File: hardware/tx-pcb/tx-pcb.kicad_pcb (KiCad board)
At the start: 4 copper layers, 83.4 x 79.1 mm, 66 parts, among them J1 Conn_To_J1, J2 Conn_To_J2, J3 BLIO, J4 Conn_01x05, J5 Conn_01x04, J6 PWRO, J7 Conn_01x02_Pin, SW1 BOOT0, SW2 RESET, SW3 BTN1, SW4 BTN2, SW5 BTN3, SW6 BTN4, SW7 BTN5, SW8 SW_SPDT, U1 USBLC6-2SC6, U2 STM32WB55CEUx, X1 CS11336-32M, X2 ABS07-32.768KHZ-1-T

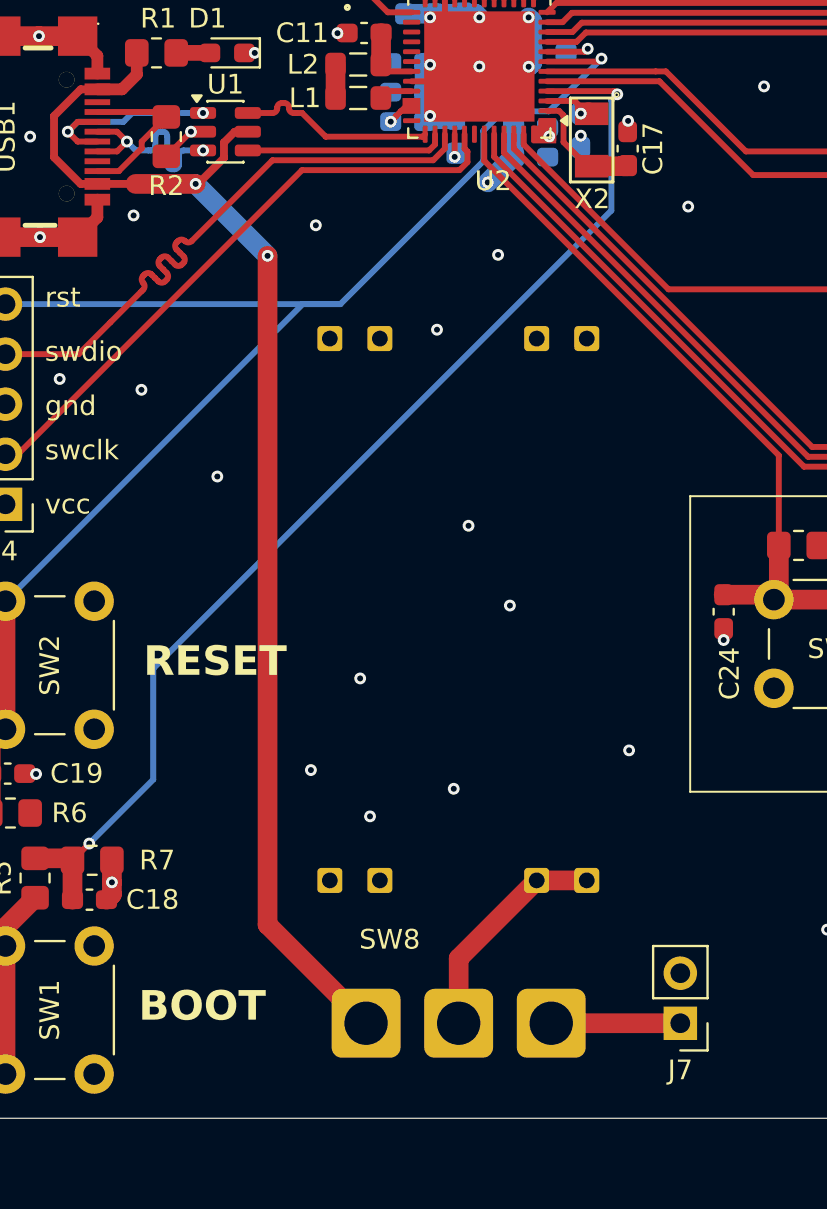
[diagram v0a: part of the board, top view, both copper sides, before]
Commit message: updated power switch for tx board
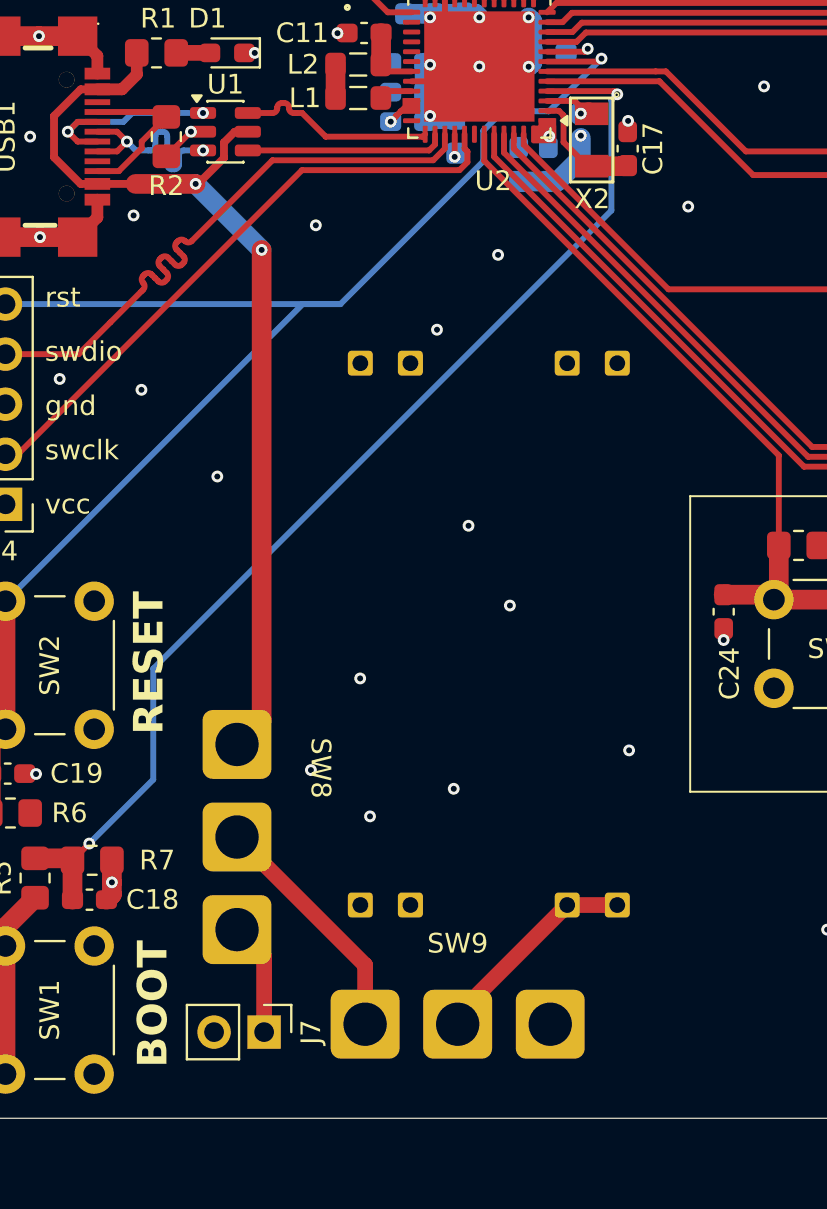
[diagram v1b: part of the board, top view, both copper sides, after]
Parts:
- added SW9: SW_SPDT, rf-pwr-tx-library:spdt_amazon, F.Cu at (146.7, 135.3)
- moved J7 21.1 mm to (136.9, 135.7), turned to -90 degrees
- moved SW8 14.7 mm to (135.5, 125.8), turned to 90 degrees
- moved U3 1.99 mm to (148.3, 115.5)
- moved C6 1.97 mm to (149.8, 91.7), turned to -90 degrees
- moved C5 0.97 mm to (151.3, 91.7), turned to -90 degrees
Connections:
- SW8 pad 2: /reg_in -> Net-(SW8-B)
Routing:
- net /VBUS: track 66.4 -> 50.6 mm
- net Net-(SW8-B): track 0.00 -> 12.2 mm
- net GND: track 45.3 -> 46.6 mm, vias 47 -> 46
- net Net-(J7-Pin_1): track 6.55 -> 5.77 mm
- net /reg_in: track 11.4 -> 10.9 mm

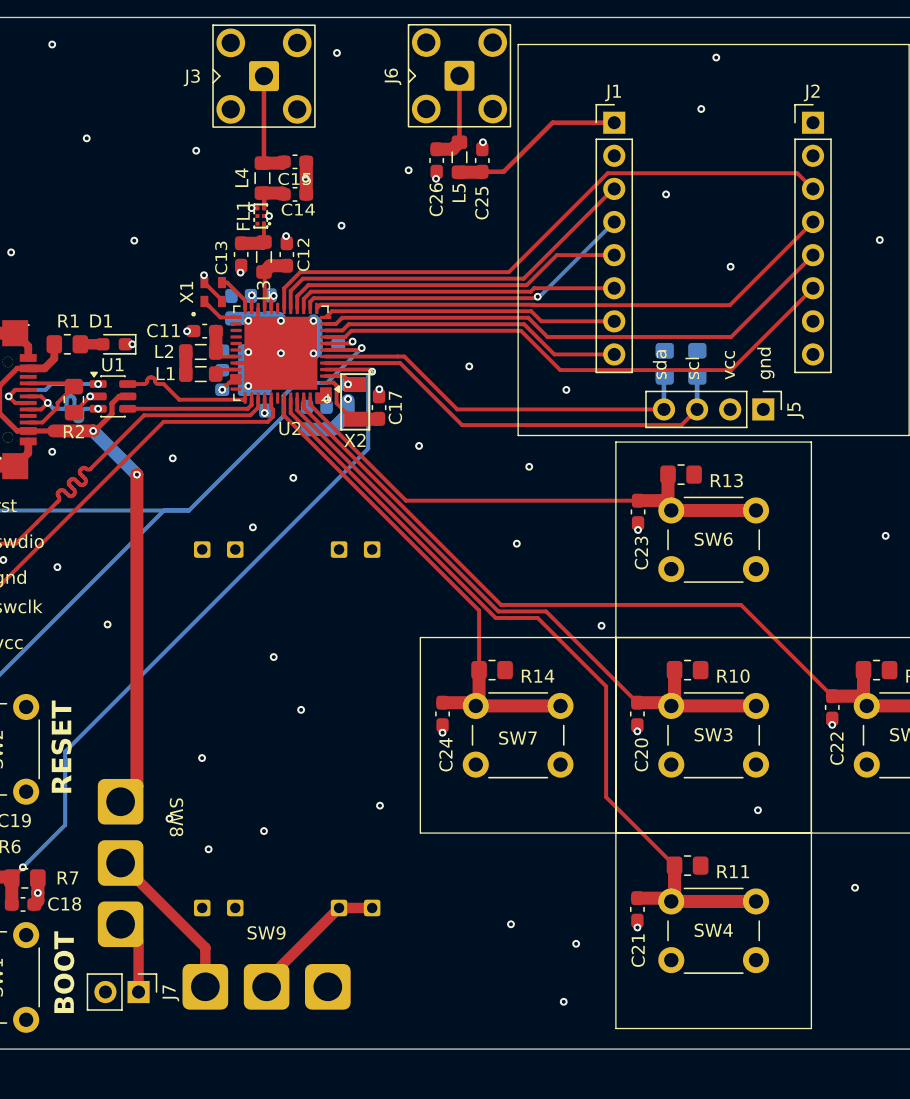
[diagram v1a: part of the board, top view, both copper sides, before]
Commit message: double checked for purchase
updated TX SPI_CLK pin, was incorrect
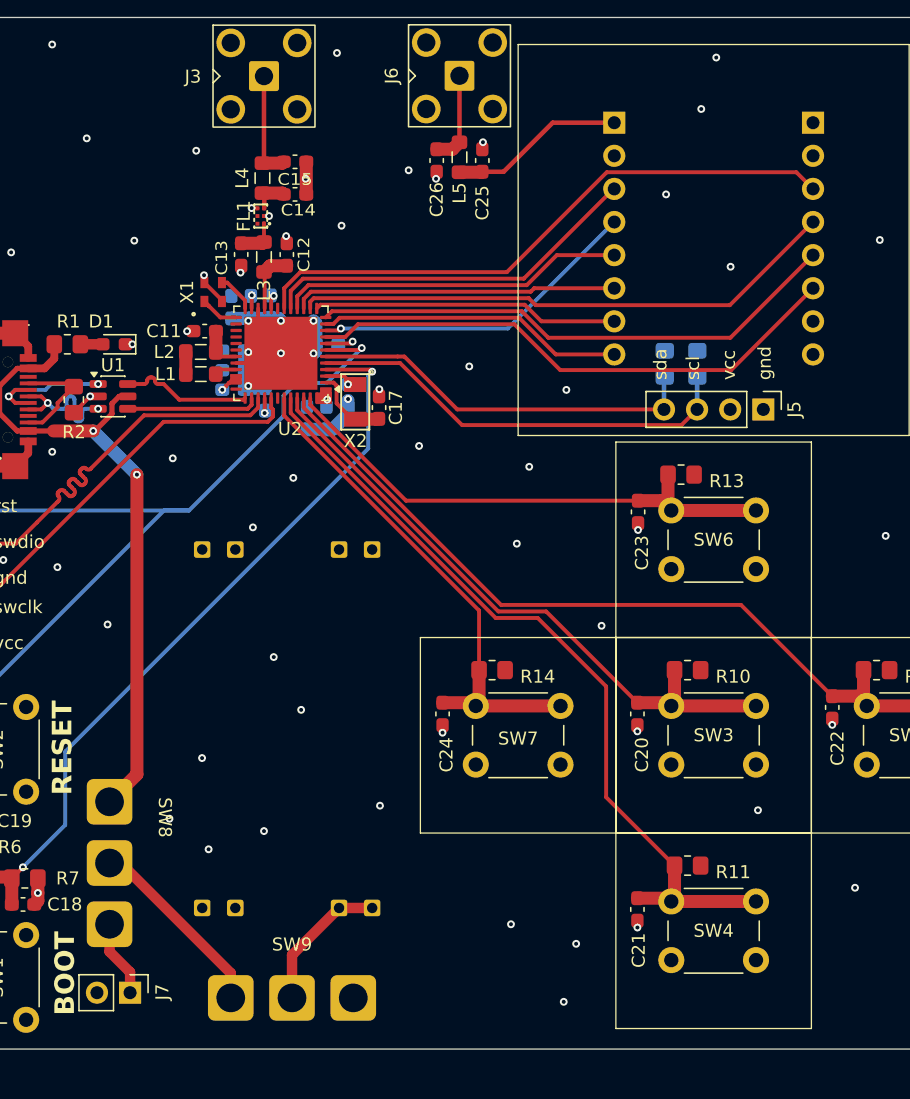
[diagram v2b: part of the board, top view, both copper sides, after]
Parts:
- J1, J2: moved to B.Cu
- moved SW9 2.13 mm to (148.7, 136.2)
- moved SW8 0.85 mm to (134.7, 125.8)
- moved J7 0.65 mm to (136.2, 135.8)
- turned J1 to 180 degrees
- turned J2 to 180 degrees
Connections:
- U2 pad 10: /SX1262_BUSY -> /SPI_SCK
- U2 pad 11: /SX1262_DIO2 -> /SX1262_BUSY
- U2 pad 12: /SX1262_RST -> /SX1262_DIO2
- U2 pad 13: /SX1262_RFSW -> /SX1262_RST
- U2 pad 14: /SPI_SCK -> /SX1262_RFSW
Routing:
- net Net-(SW8-B): track 12.2 -> 13.9 mm
- net /SX1262_RFSW: track 40.9 -> 42.1 mm
- net /SX1262_RST: track 22.7 -> 23.5 mm
- net /SPI_SCK: track 26.4 -> 25.6 mm

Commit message: updates immediately pre JLC
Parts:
- moved J7 14.2 mm to (150.4, 135.2), turned to 0 degrees
- moved SW9 11.7 mm to (160.4, 135.8)
- moved SW8 11.4 mm to (140.2, 135.8), turned to 180 degrees
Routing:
- net /VBUS: track 50.6 -> 65.2 mm
- net Net-(SW8-B): track 13.9 -> 18.0 mm
- net /reg_in: track 10.9 -> 11.7 mm
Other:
- board text added: "-"
- board text added: "BAT"
- board text added: "O"
- board text added: "USB"

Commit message: updates for dr weeks
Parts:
- removed D1: LED, LED_SMD:LED_0603_1608Metric_Pad1.05x0.95mm_HandSolder
- removed R1: 10k, Resistor_SMD:R_0805_2012Metric_Pad1.20x1.40mm_HandSolder
- removed R2: 5k1, Resistor_SMD:R_0805_2012Metric_Pad1.20x1.40mm_HandSolder
- removed SW8: SW_SPDT, rf-pwr-tx-library:spdt_amazon
- removed U1: USBLC6-2SC6, Package_TO_SOT_SMD:SOT-23-6
- removed USB1: GT-USB-7047A, rf-pwr-tx-library:USB-C-SMD_GT-USB-7047A
- moved U3 36.5 mm to (181.1, 131.6), turned to 180 degrees
- moved J7 12.5 mm to (162.8, 135.2)
- moved C18 8.61 mm to (136.6, 129.0)
- moved J4 8.61 mm to (132.4, 108.9)
- moved R5 8.61 mm to (133.9, 127.9)
- moved R6 8.61 mm to (132.6, 124.6)
- moved SW1 8.61 mm to (132.4, 137.8)
- moved SW2 8.61 mm to (132.4, 120.3)
- moved C19 8.61 mm to (132.5, 122.6)
- moved R7 8.61 mm to (136.8, 127.0)
- moved SW9 7.75 mm to (152.6, 135.8)
- moved C6 1.81 mm to (149.8, 89.9), turned to 90 degrees
- moved C5 1.81 mm to (151.3, 89.9), turned to 90 degrees
- moved C2 0.76 mm to (146.6, 89.5)
- moved C1 0.35 mm to (151.3, 85.6)
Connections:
- SW9 pad 3: Net-(SW8-B) -> Net-(J7-Pin_1)
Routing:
- net /VBUS: track 65.2 -> 0.00 mm, vias 2 -> 0
- net GND: track 46.6 -> 26.9 mm, vias 46 -> 39
- net Net-(SW8-B): track 18.0 -> 0.00 mm
- net /SWD_NSRT: track 73.4 -> 61.1 mm
- net /SWDIO: track 30.9 -> 18.7 mm
- net /reg_in: track 11.7 -> 0.00 mm
- net Net-(USB1-DN1): track 10.7 -> 0.00 mm, vias 2 -> 0
- net Net-(USB1-DP1): track 10.6 -> 0.00 mm, vias 2 -> 0
- net /USB_DP: track 10.1 -> 0.00 mm
- net /USB_DM: track 10.1 -> 0.00 mm
- net /SWCLK: track 31.1 -> 22.5 mm
- net Net-(USB1-CC1): track 8.44 -> 0.00 mm
- net Net-(J7-Pin_1): track 5.74 -> 0.00 mm
- net /BTN2: track 62.0 -> 65.7 mm
- net /BOOT0: track 57.9 -> 54.4 mm
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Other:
- board size 83.4 x 79.1 mm -> 74.3 x 79.1 mm
- board text removed: "BAT"
- board text removed: "USB"

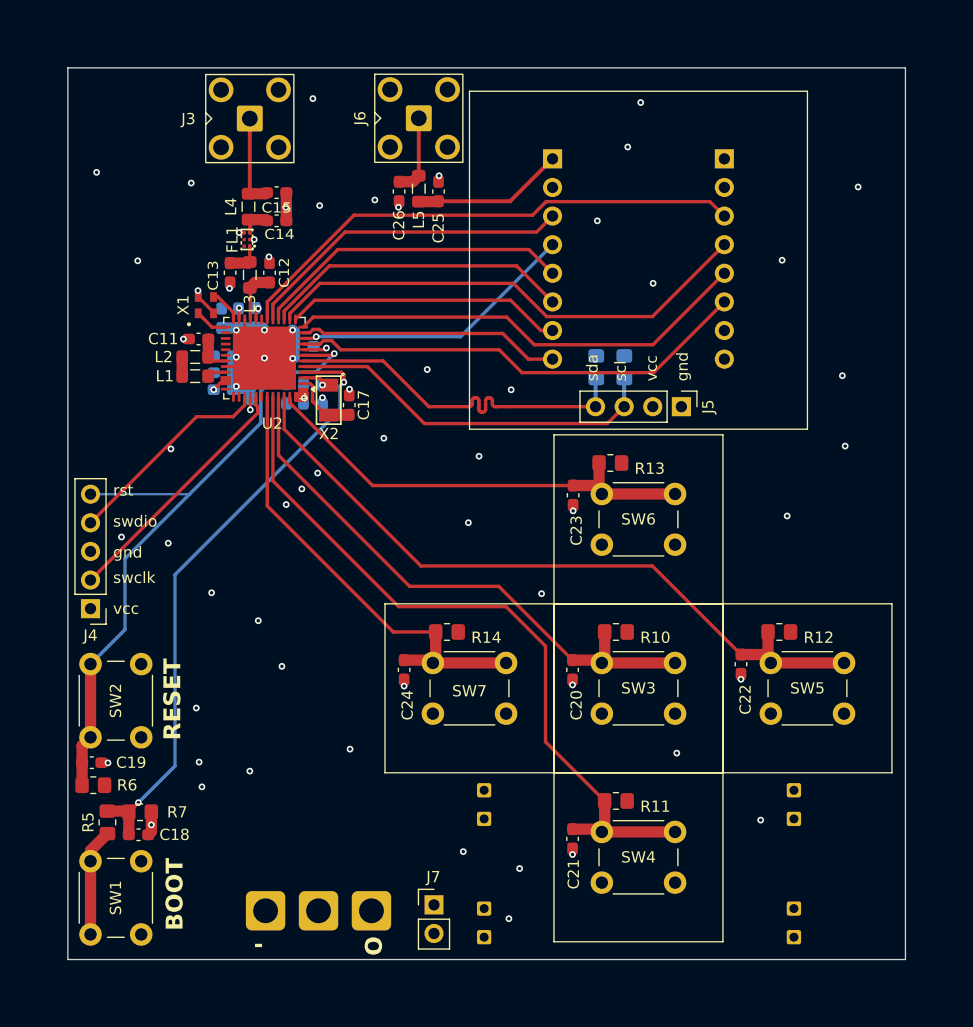
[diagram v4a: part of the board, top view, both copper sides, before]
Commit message: updated PCB for weeks purchase
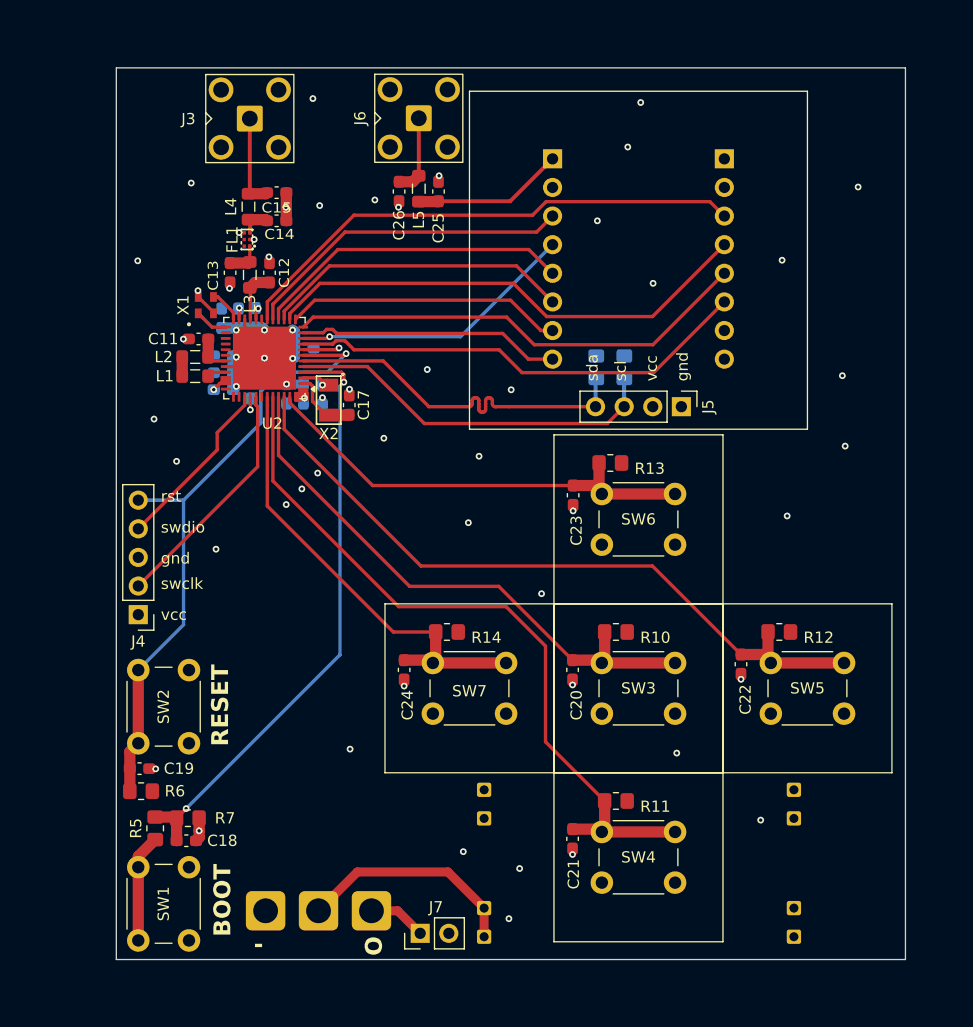
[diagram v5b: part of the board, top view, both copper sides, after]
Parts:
- moved C18 4.27 mm to (140.9, 129.5)
- moved C19 4.27 mm to (136.7, 123.1)
- moved R7 4.27 mm to (141.0, 127.5)
- moved R5 4.27 mm to (138.1, 128.4)
- moved R6 4.27 mm to (136.8, 125.1)
- moved SW1 4.27 mm to (136.6, 138.4)
- moved SW2 4.27 mm to (136.6, 120.9)
- moved J4 4.27 mm to (136.6, 109.5)
- moved J7 2.81 mm to (161.6, 137.8), turned to 90 degrees
- moved C1 0.16 mm to (151.3, 85.8)
- moved C2 0.06 mm to (146.6, 89.4)
- turned SW9 to 0 degrees
- turned U3 to 0 degrees
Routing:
- net /reg_in: track 0.00 -> 20.0 mm
- net Net-(J7-Pin_1): track 0.00 -> 5.15 mm
- net /SWD_NSRT: track 61.1 -> 57.2 mm
- net /SWDIO: track 18.7 -> 15.6 mm
- net GND: track 26.9 -> 28.5 mm, vias 39 -> 36
- net /BOOT0: track 54.4 -> 53.2 mm
- net /SWCLK: track 22.5 -> 21.3 mm
- net +3V3: track 7.36 -> 8.12 mm, vias 32 -> 28
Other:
- board size 74.3 x 79.1 mm -> 70 x 79.1 mm

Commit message: fixed HSE induction loop
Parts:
- X1: value CS11336-32M -> Q22FA12800025; footprint rf-pwr-tx-library:NX2016SA_NDK -> easyeda2kicad:CRYSTAL-SMD_4P-L2.0-W1.6-BL
- moved C7 1.28 mm to (143.1, 84.1), turned to 0 degrees
- moved X1 0.06 mm to (142.7, 82.0), turned to 0 degrees
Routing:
- net GND: track 28.5 -> 26.5 mm, vias 36 -> 37
- net /HSE_OSC_IN: track 3.48 -> 2.15 mm
- net /HSE_OSC_OUT: track 2.96 -> 2.15 mm
